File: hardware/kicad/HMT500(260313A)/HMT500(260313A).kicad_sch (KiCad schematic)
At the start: 0 parts

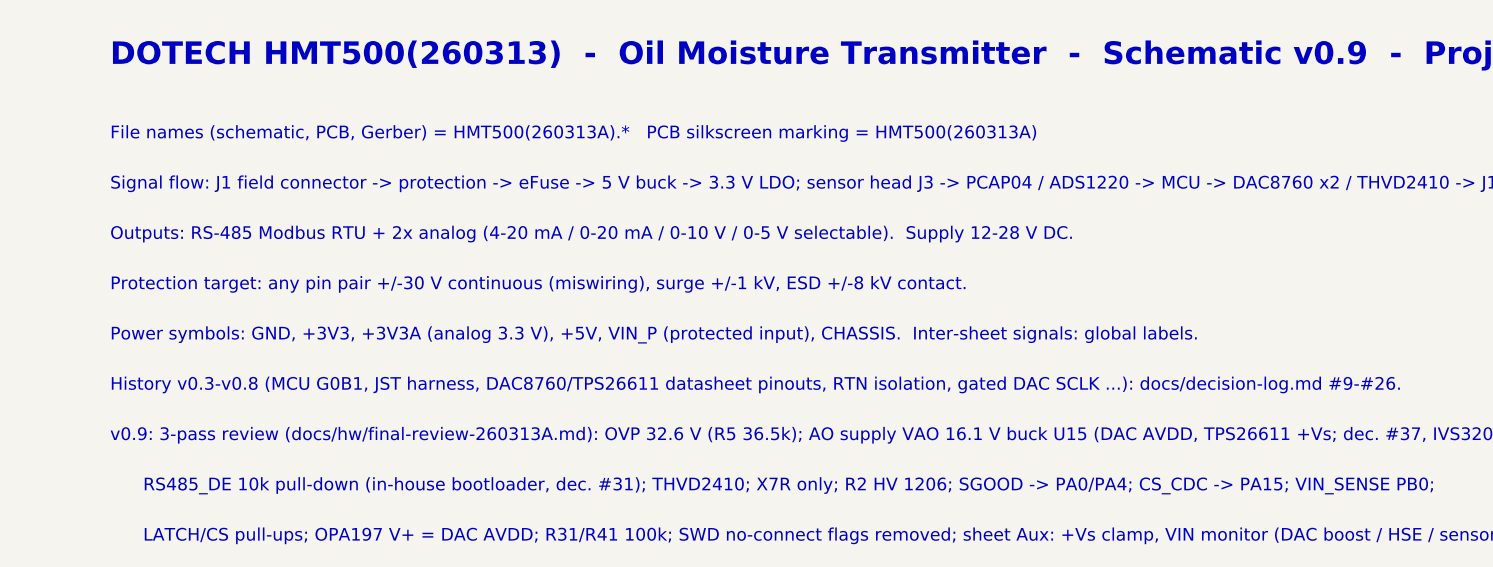
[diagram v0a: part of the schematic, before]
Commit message: 회로 v0.10: AO D30/D40을 TVS1401 14 V로 변경
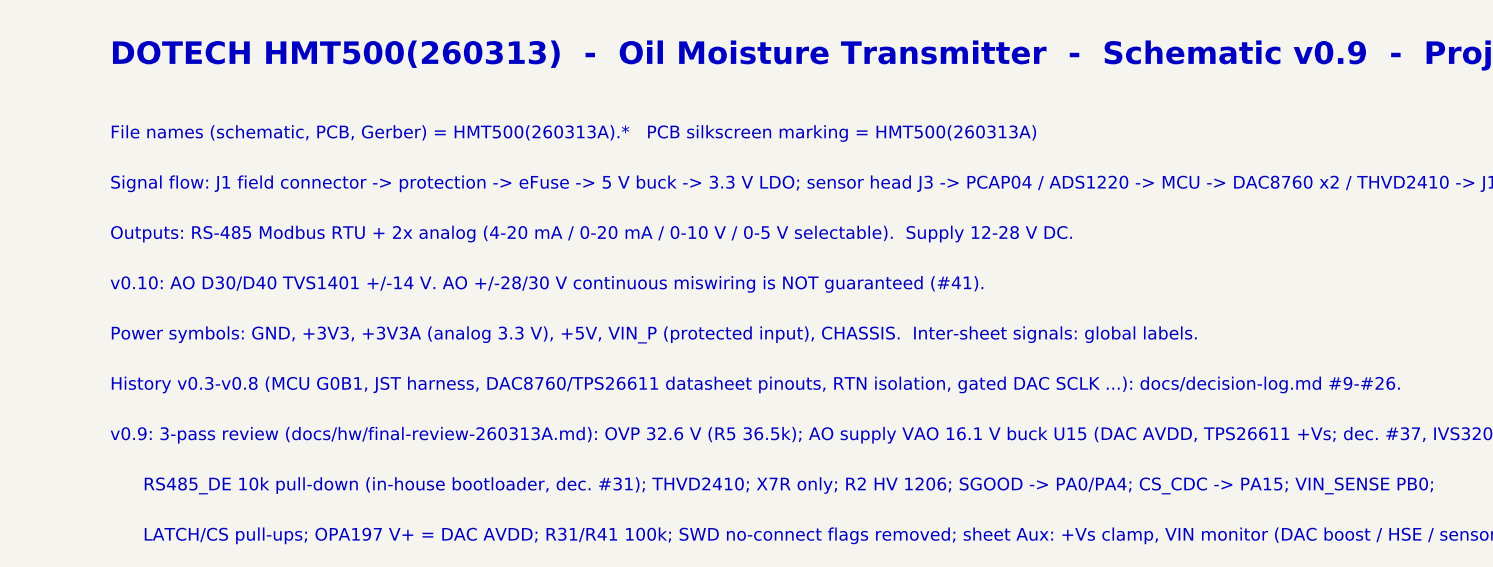
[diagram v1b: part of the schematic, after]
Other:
- note added: "v0.10: AO D30/D40 TVS1401 +/-14 V. AO +/-28/30 V continuous miswiring is NOT guaranteed (#41)."
- note removed: "Protection target: any pin pair +/-30 V continuous (miswiring), surge +/-1 kV, ESD +/-8 kV contact."
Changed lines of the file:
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@@
 (kicad_sch (version 20230121) (generator eeschema) (paper "A3")
-(title_block (title "HMT500(260313A)  Top") (date "2026-09-30") (rev "0.9") (company "DOTECH Co., Ltd.") (comment 1 "Project No. HMT500(260313A)  -  HMT500(260313) oil moisture transmitter") (comment 2 "Design notes: docs/hw/circuit-design.md") (comment 3 "Pinouts checked vs manufacturer datasheets 2026-09-30 (STM32: KiCad lib)"))
+(title_block (title "HMT500(260313A)  Top") (date "2026-10-01") (rev "0.10") (company "DOTECH Co., Ltd.") (comment 1 "Project No. HMT500(260313A)  -  HMT500(260313) oil moisture transmitter") (comment 2 "Design notes: docs/hw/circuit-design.md") (comment 3 "Pinouts checked vs manufacturer datasheets 2026-09-30 (STM32: KiCad lib)"))
 (sheet (at 20.32 35.56) (size 86.36 40.64) (fields_autoplaced) (stroke (width 0.1524) (type solid)) (fill (color 0 0 0 0.0000)) (property "Sheetname" "1. Connector & input protection" (at 20.32 34.798 0) (effects (font (size 1.8 1.8) bold) (justify left bottom))) (property "Sheetfile" "HMT500(260313A)_connector.kicad_sch" (at 20.32 76.962 0) (effects (font (size 1.27 1.27)) (justify left top))) (instances (project "HMT500(260313A)" (path "/1ebb025b-11bd-5f7c-aaab-41e2a750e8b3" (page "2")))))
 (text "Field connector, 2-stage bidirectional" (at 22.86 50.8 0) (effects (font (size 1.4 1.4)) (justify left bottom)))
@@
 (text "Signal flow: J1 field connector -> protection -> eFuse -> 5 V buck -> 3.3 V LDO; sensor head J3 -> PCAP04 / ADS1220 -> MCU -> DAC8760 x2 / THVD2410 -> J1" (at 30.48 161.036 0) (effects (font (size 1.4 1.4)) (justify left bottom)))
 (text "Outputs: RS-485 Modbus RTU + 2x analog (4-20 mA / 0-20 mA / 0-10 V / 0-5 V selectable).  Supply 12-28 V DC." (at 30.48 166.624 0) (effects (font (size 1.4 1.4)) (justify left bottom)))
-(text "Protection target: any pin pair +/-30 V continuous (miswiring), surge +/-1 kV, ESD +/-8 kV contact." (at 30.48 172.212 0) (effects (font (size 1.4 1.4)) (justify left bottom)))
+(text "v0.10: AO D30/D40 TVS1401 +/-14 V. AO +/-28/30 V continuous miswiring is NOT guaranteed (#41)." (at 30.48 172.212 0) (effects (font (size 1.4 1.4)) (justify left bottom)))
 (text "Power symbols: GND, +3V3, +3V3A (analog 3.3 V), +5V, VIN_P (protected input), CHASSIS.  Inter-sheet signals: global labels." (at 30.48 177.8 0) (effects (font (size 1.4 1.4)) (justify left bottom)))
 (text "History v0.3-v0.8 (MCU G0B1, JST harness, DAC8760/TPS26611 datasheet pinouts, RTN isolation, gated DAC SCLK ...): docs/decision-log.md #9-#26." (at 30.48 183.388 0) (effects (font (size 1.4 1.4)) (justify left bottom)))
